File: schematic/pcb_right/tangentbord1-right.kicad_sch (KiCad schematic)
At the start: 24 parts, among them J1 UART, J2 DBG

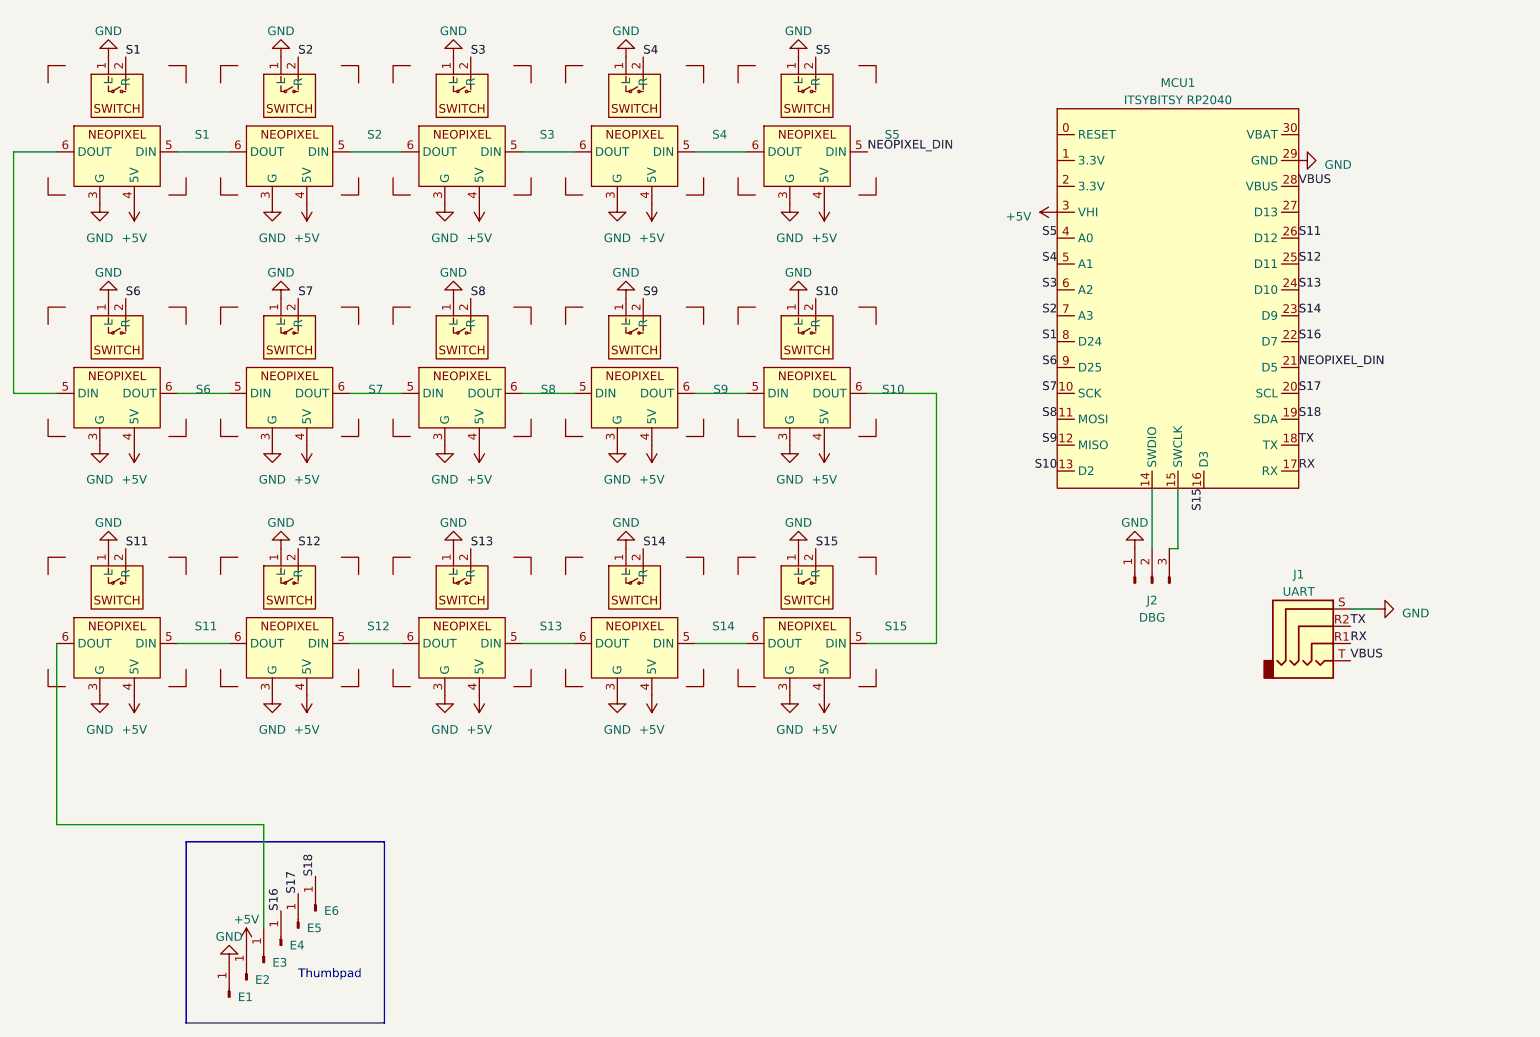
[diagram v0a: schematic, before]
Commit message: Tweak left PCB, add right & thumb PCB
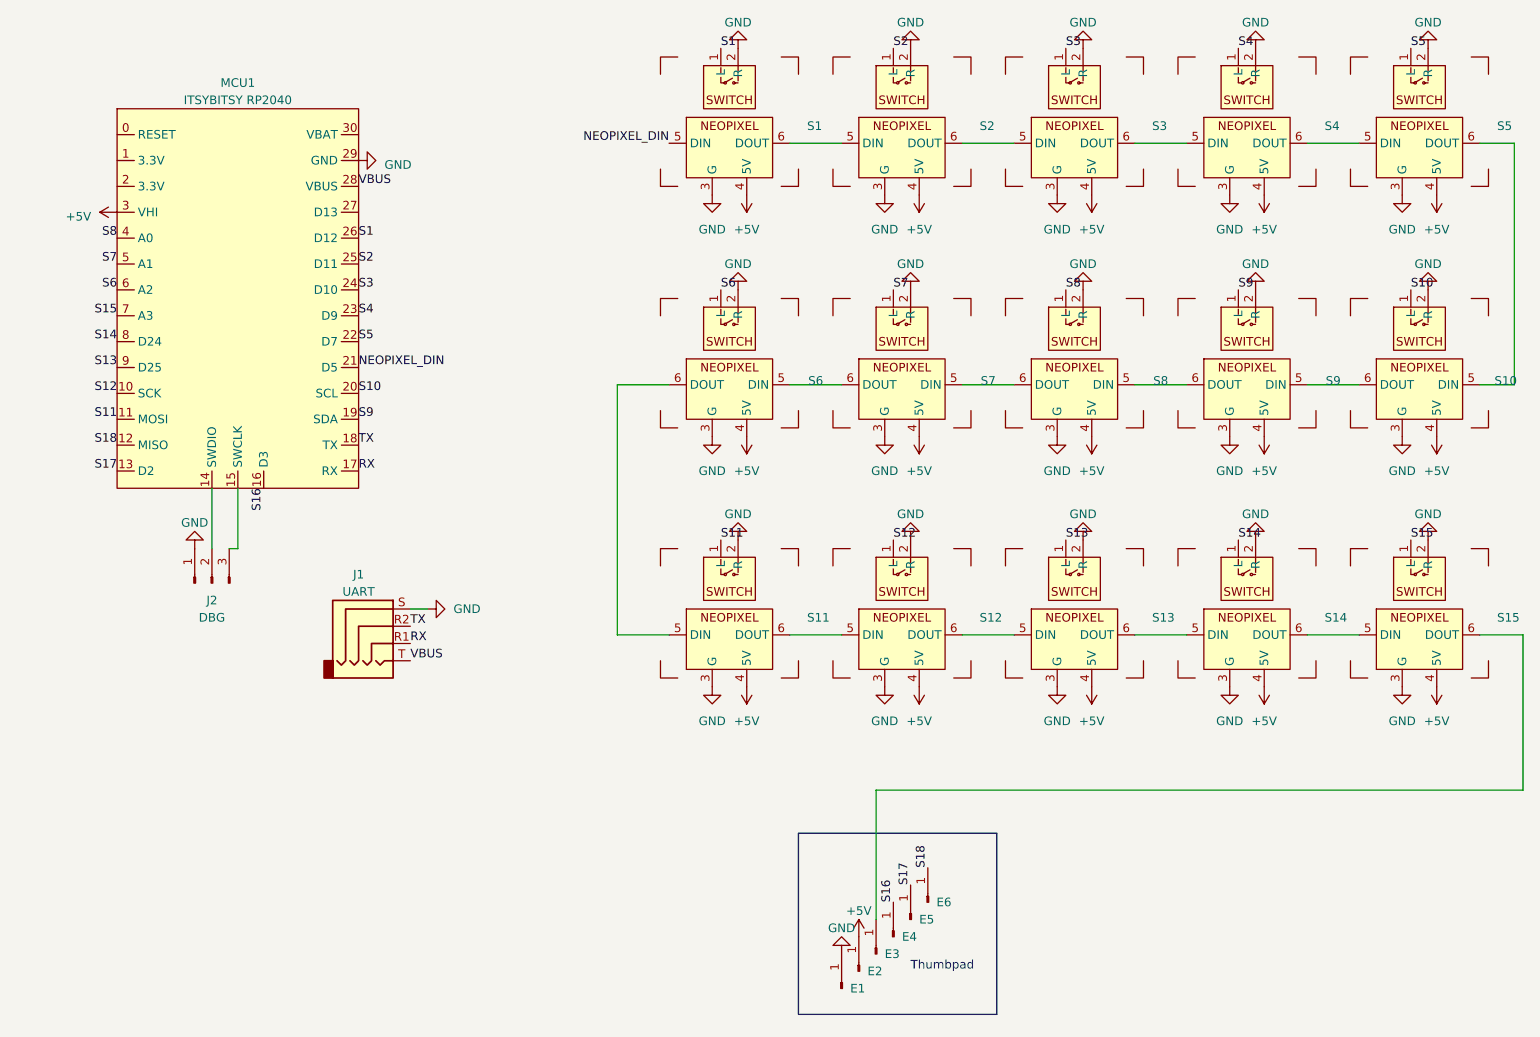
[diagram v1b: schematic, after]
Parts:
- S1, S11, S12, S13, S14, S15, S2, S3, S4, S5: footprint Footprints:MX_SW_SOCKET_LED -> Footprints:MX_SW_SOCKET_LED_REV; symbol library:MX_SW_SOCKET_RGB -> library:MX_SW_SOCKET_RGB_REV
- S10, S6, S7, S8, S9: footprint Footprints:MX_SW_SOCKET_LED_REV -> Footprints:MX_SW_SOCKET_LED; symbol library:MX_SW_SOCKET_RGB_REV -> library:MX_SW_SOCKET_RGB
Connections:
- net GND: now also S1.2 (R), S10.2 (R), S11.2 (R), S12.2 (R), S13.2 (R), S14.2 (R), S15.2 (R), S2.2 (R), S3.2 (R), S4.2 (R), S5.2 (R), S6.2 (R), S7.2 (R), S8.2 (R), S9.2 (R); no longer S1.1 (L), S10.1 (L), S11.1 (L), S12.1 (L), S13.1 (L), S14.1 (L), S15.1 (L), S2.1 (L), S3.1 (L), S4.1 (L), S5.1 (L), S6.1 (L), S7.1 (L), S8.1 (L), S9.1 (L)
- net NEOPIXEL_DIN: now also S1.5 (DIN); no longer S5.5 (DIN)
- net S1: now also MCU1.26 (D12), S1.1 (L); no longer MCU1.8 (D24), S1.2 (R)
- net S10: now also MCU1.20 (SCL), S10.1 (L); no longer MCU1.13 (D2), S10.2 (R)
- net S11: now also MCU1.11 (MOSI), S11.1 (L); no longer MCU1.26 (D12), S11.2 (R)
- net S12: now also MCU1.10 (SCK), S12.1 (L); no longer MCU1.25 (D11), S12.2 (R)
- net S13: now also MCU1.9 (D25), S13.1 (L); no longer MCU1.24 (D10), S13.2 (R)
- net S14: now also MCU1.8 (D24), S14.1 (L); no longer MCU1.23 (D9), S14.2 (R)
- net S15: now also MCU1.7 (A3), S15.1 (L); no longer MCU1.16 (D3), S15.2 (R)
- net S16: now also MCU1.16 (D3); no longer MCU1.22 (D7)
- net S17: now also MCU1.13 (D2); no longer MCU1.20 (SCL)
- net S18: now also MCU1.12 (MISO); no longer MCU1.19 (SDA)
- net S2: now also MCU1.25 (D11), S2.1 (L); no longer MCU1.7 (A3), S2.2 (R)
- net S3: now also MCU1.24 (D10), S3.1 (L); no longer MCU1.6 (A2), S3.2 (R)
- net S4: now also MCU1.23 (D9), S4.1 (L); no longer MCU1.5 (A1), S4.2 (R)
- net S5: now also MCU1.22 (D7), S5.1 (L); no longer MCU1.4 (A0), S5.2 (R)
- net S6: now also MCU1.6 (A2), S6.1 (L); no longer MCU1.9 (D25), S6.2 (R)
- net S7: now also MCU1.5 (A1), S7.1 (L); no longer MCU1.10 (SCK), S7.2 (R)
- net S8: now also MCU1.4 (A0), S8.1 (L); no longer MCU1.11 (MOSI), S8.2 (R)
- net S9: now also MCU1.19 (SDA), S9.1 (L); no longer MCU1.12 (MISO), S9.2 (R)
- net at S4.5 (DIN): now also S3.6 (DOUT); no longer S5.6 (DOUT)
- net at S4.6 (DOUT): now also S5.5 (DIN); no longer S3.5 (DIN)
- net at S6.5 (DIN): now also S7.6 (DOUT); no longer S1.6 (DOUT)
- net at S6.6 (DOUT): now also S11.5 (DIN); no longer S7.5 (DIN)
- net at S14.5 (DIN): now also S13.6 (DOUT); no longer S15.6 (DOUT)
- net at S14.6 (DOUT): now also S15.5 (DIN); no longer S13.5 (DIN)
- net at E3.1 (Pin_1): now also S15.6 (DOUT); no longer S11.6 (DOUT)
- net at S12.5 (DIN): now also S11.6 (DOUT); no longer S13.6 (DOUT)
- net at S12.6 (DOUT): now also S13.5 (DIN); no longer S11.5 (DIN)
- net at S2.6 (DOUT): now also S3.5 (DIN); no longer S1.5 (DIN)
- net at S9.5 (DIN): now also S10.6 (DOUT); no longer S8.6 (DOUT)
- net at S9.6 (DOUT): now also S8.5 (DIN); no longer S10.5 (DIN)
- net at S2.5 (DIN): now also S1.6 (DOUT); no longer S3.6 (DOUT)
- new net: S7.5 (DIN), S8.6 (DOUT)
- new net: S10.5 (DIN), S5.6 (DOUT)
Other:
- moved on the sheet: E1, E2, E3, E4, E5, E6, J1, J2, MCU1, S1, S10, S11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

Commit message: Swap RX/TX on pcb_right
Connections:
- net RX: now also J1.R2; no longer J1.R1
- net TX: now also J1.R1; no longer J1.R2
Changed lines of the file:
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@@
     (effects (font (size 1.27 1.27)) (justify left bottom))
   )
-  (label "RX" (at 80.01 111.76 0) (fields_autoplaced)
+  (label "RX" (at 80.01 109.22 0) (fields_autoplaced)
     (effects (font (size 1.27 1.27)) (justify left bottom))
   )
@@
     (effects (font (size 1.27 1.27)) (justify left bottom))
   )
-  (label "TX" (at 80.01 109.22 0) (fields_autoplaced)
+  (label "TX" (at 80.01 111.76 0) (fields_autoplaced)
     (effects (font (size 1.27 1.27)) (justify left bottom))
   )
